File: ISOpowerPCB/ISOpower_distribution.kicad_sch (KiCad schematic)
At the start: 27 parts, among them M1 Fan_IEC60617, Q2 IRF5305_PBF, Q3 IRF5305_PBF, U10 LM2596S-5, U4 i6A4W020A-DC-DC-250W, U5 i6A4W020A-DC-DC-250W, U6 ACS712xLCTR-30A, U7 ACS712xLCTR-30A

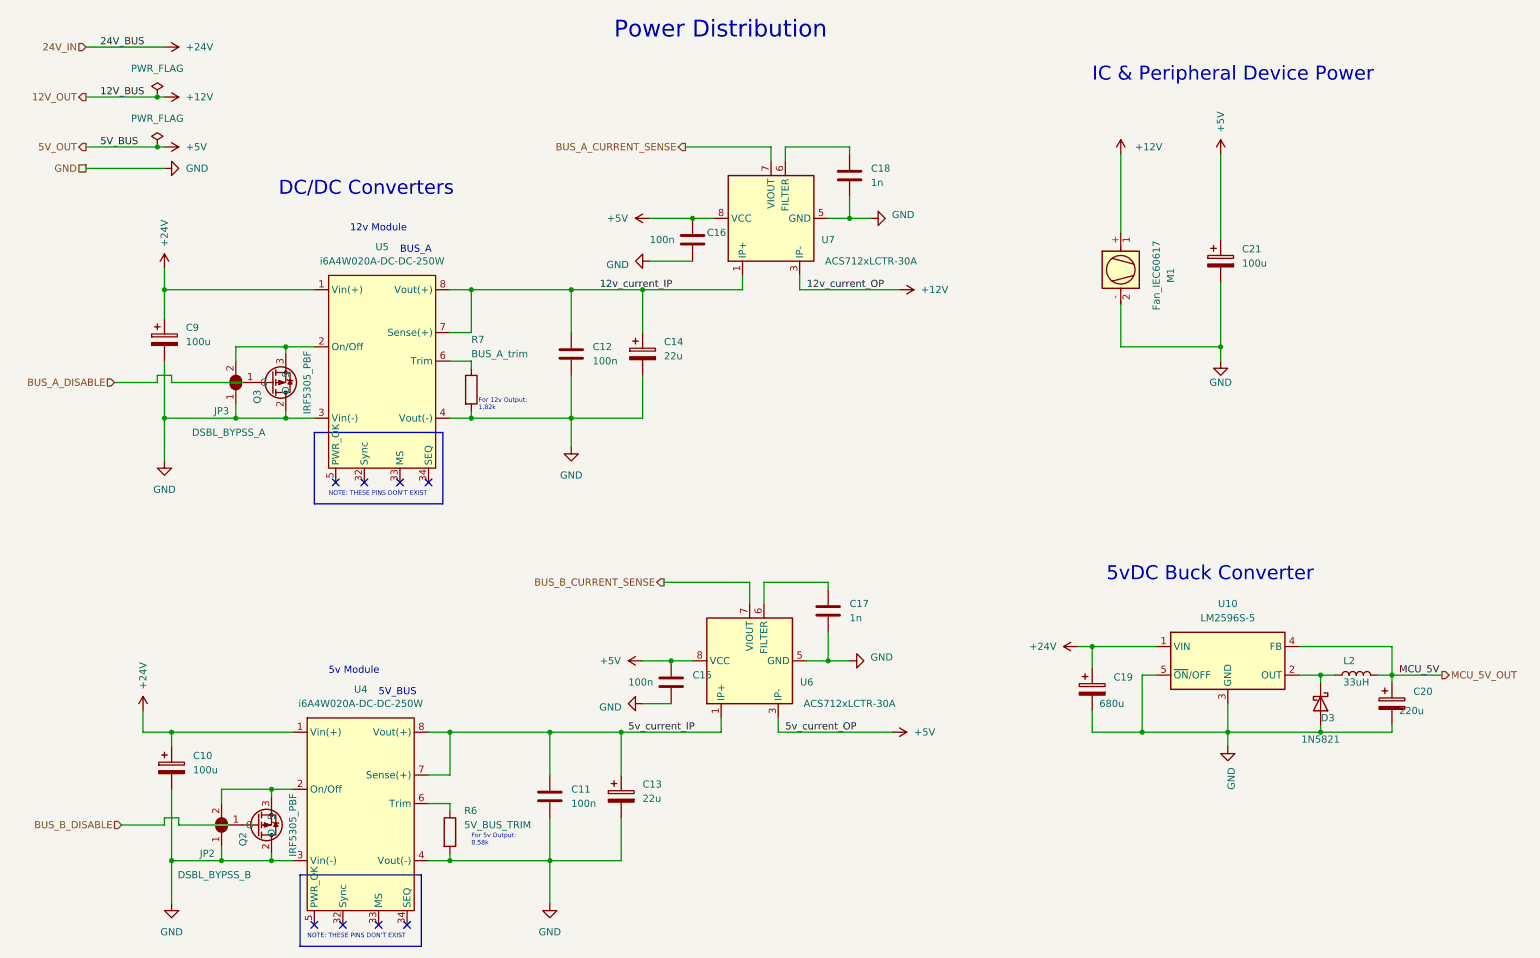
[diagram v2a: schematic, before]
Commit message: added netclasses
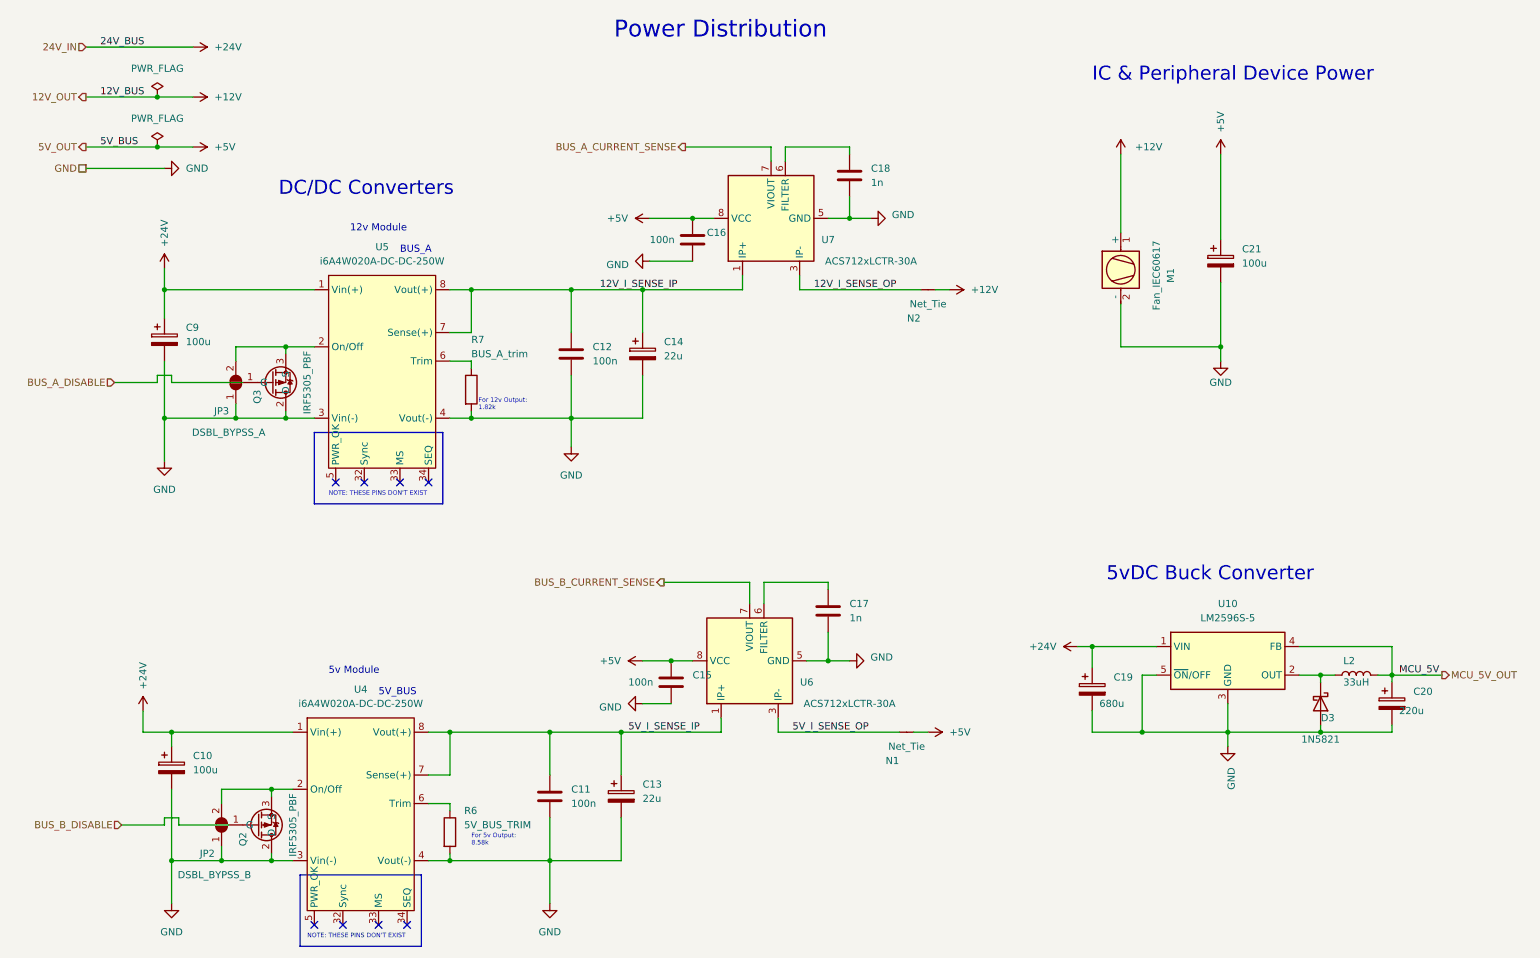
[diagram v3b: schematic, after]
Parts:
- added N1, N2: Net_Tie, NetTie:NetTie-2_SMD_Pad0.5mm, symbol 000_Utility_Immo:Net_Tie
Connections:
- net +12V: now also N2.2 (C); no longer U7.3 (IP-), U7.4 (IP-)
- net +5V: now also N1.2 (C); no longer U6.3 (IP-), U6.4 (IP-)
- net 12v_current_IP renamed 12V_I_SENSE_IP
- net 5v_current_IP renamed 5V_I_SENSE_IP
- new net 12V_I_SENSE_OP: N2.1 (A), U7.3 (IP-), U7.4 (IP-)
- new net 5V_I_SENSE_OP: N1.1 (A), U6.3 (IP-), U6.4 (IP-)
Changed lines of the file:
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@@
     (stroke (width 0) (type default) (color 0 0 0 0))
   )
-  (wire (pts (xy 149.86 143.51) (xy 170.18 143.51))
+  (wire (pts (xy 149.86 143.51) (xy 171.45 143.51))
     (stroke (width 0) (type default) (color 0 0 0 0))
   )
@@
     (stroke (width 0) (type default) (color 0 0 0 0))
   )
-  (wire (pts (xy 26.67 21.59) (xy 40.64 21.59))
+  (wire (pts (xy 26.67 21.59) (xy 45.72 21.59))
     (stroke (width 0) (type default) (color 0 0 0 0))
   )
@@
     (stroke (width 0) (type default) (color 0 0 0 0))
   )
-  (wire (pts (xy 153.67 64.77) (xy 171.45 64.77))
+  (wire (pts (xy 153.67 64.77) (xy 175.26 64.77))
     (stroke (width 0) (type default) (color 0 0 0 0))
   )
@@
     (stroke (width 0) (type default) (color 0 0 0 0))
   )
+  (wire (pts (xy 176.53 143.51) (xy 173.99 143.51))
+    (stroke (width 0) (type default) (color 0 0 0 0))
+  )
   (wire (pts (xy 59.69 165.1) (xy 59.69 166.37))
     (stroke (width 0) (type default) (color 0 0 0 0))
@@
     (stroke (width 0) (type default) (color 0 0 0 0))
   )
-  (wire (pts (xy 39.37 39.37) (xy 40.64 39.37))
+  (wire (pts (xy 39.37 39.37) (xy 45.72 39.37))
     (stroke (width 0) (type default) (color 0 0 0 0))
   )
@@
     (stroke (width 0) (type default) (color 0 0 0 0))
   )
-  (wire (pts (xy 39.37 30.48) (xy 40.64 30.48))
+  (wire (pts (xy 39.37 30.48) (xy 45.72 30.48))
     (stroke (width 0) (type default) (color 0 0 0 0))
   )
@@
   )
   (wire (pts (xy 158.75 118.11) (xy 158.75 116.84))
+    (stroke (width 0) (type default) (color 0 0 0 0))
+  )
+  (wire (pts (xy 180.34 64.77) (xy 177.8 64.77))
     (stroke (width 0) (type default) (color 0 0 0 0))
   )
@@
     (effects (font (size 1.27 1.27)) (justify left bottom))
   )
-  (label "12v_current_IP" (at 118.11 64.77 0)
+  (label "12V_I_SENSE_IP" (at 118.11 64.77 0)
     (effects (font (size 1.27 1.27)) (justify left bottom))
   )
-  (label "5v_current_OP" (at 151.13 143.51 0)
+  (label "12V_I_SENSE_OP" (at 156.21 64.77 0)
     (effects (font (size 1.27 1.27)) (justify left bottom))
   )
-  (label "12v_current_OP" (at 154.94 64.77 0)
+  (label "5V_I_SENSE_OP" (at 152.4 143.51 0)
     (effects (font (size 1.27 1.27)) (justify left bottom))
   )
@@
     (effects (font (size 1.27 1.27)) (justify left bottom))
   )
-  (label "5v_current_IP" (at 123.19 143.51 0)
+  (label "5V_I_SENSE_IP" (at 123.19 143.51 0)
     (effects (font (size 1.27 1.27)) (justify left bottom))
   )
@@
     (pin "1")
   )
-  (symbol (lib_id "power:+5V") (at 170.18 143.51 270) (unit 1)
-    (in_bom yes) (on_board yes)
-    (property "Reference" "#PWR043" (id 0) (at 166.37 143.51 0)
-      (effects (font (size 1.27 1.27)) hide)
-    )
-    (property "Value" "+5V" (id 1) (at 177.8 143.51 90)
-      (effects (font (size 1.27 1.27)) (justify right))
-    )
-    (property "Footprint" "" (id 2) (at 170.18 143.51 0)
-      (effects (font (size 1.27 1.27)) hide)
-    )
-    (property "Datasheet" "" (id 3) (at 170.18 143.51 0)
-      (effects (font (size 1.27 1.27)) hide)
-    )
-    (pin "1")
-  )
-  (symbol (lib_id "power:+24V") (at 40.64 21.59 270) (unit 1)
-    (in_bom yes) (on_board yes)
-    (property "Reference" "#PWR030" (id 0) (at 36.83 21.59 0)
-      (effects (font (size 1.27 1.27)) hide)
-    )
-    (property "Value" "+24V" (id 1) (at 44.45 21.59 90)
-      (effects (font (size 1.27 1.27)) (justify left))
-    )
-    (property "Footprint" "" (id 2) (at 40.64 21.59 0)
-      (effects (font (size 1.27 1.27)) hide)
-    )
-    (property "Datasheet" "" (id 3) (at 40.64 21.59 0)
+  (symbol (lib_id "000_Utility_Immo:Net_Tie") (at 176.53 64.77 0) (unit 1)
+    (in_bom no) (on_board yes)
+    (property "Reference" "N2" (id 0) (at 173.99 69.85 0))
+    (property "Value" "Net_Tie" (id 1) (at 176.53 67.31 0))
+    (property "Footprint" "NetTie:NetTie-2_SMD_Pad0.5mm" (id 2) (at 176.53 67.31 0)
+      (effects (font (size 1.27 1.27)) hide)
+    )
+    (property "Datasheet" "~" (id 3) (at 176.53 63.5 0)
+      (effects (font (size 1.27 1.27)) hide)
+    )
+    (pin "1")
+    (pin "2")
+  )
+  (symbol (lib_id "power:+24V") (at 45.72 21.59 270) (unit 1)
+    (in_bom yes) (on_board yes)
+    (property "Reference" "#PWR030" (id 0) (at 41.91 21.59 0)
+      (effects (font (size 1.27 1.27)) hide)
+    )
+    (property "Value" "+24V" (id 1) (at 49.53 21.59 90)
+      (effects (font (size 1.27 1.27)) (justify left))
+    )
+    (property "Footprint" "" (id 2) (at 45.72 21.59 0)
+      (effects (font (size 1.27 1.27)) hide)
+    )
+    (property "Datasheet" "" (id 3) (at 45.72 21.59 0)
       (effects (font (size 1.27 1.27)) hide)
     )
@@
     (pin "1")
   )
-  (symbol (lib_id "power:+5V") (at 40.64 39.37 270) (unit 1)
-    (in_bom yes) (on_board yes) (fields_autoplaced)
-    (property "Reference" "#PWR032" (id 0) (at 36.83 39.37 0)
-      (effects (font (size 1.27 1.27)) hide)
-    )
-    (property "Value" "+5V" (id 1) (at 44.45 39.3699 90)
-      (effects (font (size 1.27 1.27)) (justify left))
-    )
-    (property "Footprint" "" (id 2) (at 40.64 39.37 0)
-      (effects (font (size 1.27 1.27)) hide)
-    )
-    (property "Datasheet" "" (id 3) (at 40.64 39.37 0)
+  (symbol (lib_id "power:+5V") (at 45.72 39.37 270) (unit 1)
+    (in_bom yes) (on_board yes) (fields_autoplaced)
+    (property "Reference" "#PWR032" (id 0) (at 41.91 39.37 0)
+      (effects (font (size 1.27 1.27)) hide)
+    )
+    (property "Value" "+5V" (id 1) (at 49.53 39.3699 90)
+      (effects (font (size 1.27 1.27)) (justify left))
+    )
+    (property "Footprint" "" (id 2) (at 45.72 39.37 0)
+      (effects (font (size 1.27 1.27)) hide)
+    )
+    (property "Datasheet" "" (id 3) (at 45.72 39.37 0)
       (effects (font (size 1.27 1.27)) hide)
     )
@@
     (pin "2")
   )
-  (symbol (lib_id "power:+12V") (at 171.45 64.77 270) (unit 1)
-    (in_bom yes) (on_board yes) (fields_autoplaced)
-    (property "Reference" "#PWR044" (id 0) (at 167.64 64.77 0)
-      (effects (font (size 1.27 1.27)) hide)
-    )
-    (property "Value" "+12V" (id 1) (at 175.26 64.7699 90)
-      (effects (font (size 1.27 1.27)) (justify left))
-    )
-    (property "Footprint" "" (id 2) (at 171.45 64.77 0)
-      (effects (font (size 1.27 1.27)) hide)
-    )
-    (property "Datasheet" "" (id 3) (at 171.45 64.77 0)
-      (effects (font (size 1.27 1.27)) hide)
-    )
-    (pin "1")
-  )
   (symbol (lib_id "000_Capacitor_Electrolytic_Immo:22u") (at 121.92 154.94 0) (unit 1)
     (in_bom yes) (on_board yes) (fields_autoplaced)
@@
     (pin "2")
   )
-  (symbol (lib_id "power:+12V") (at 40.64 30.48 270) (unit 1)
-    (in_bom yes) (on_board yes) (fields_autoplaced)
-    (property "Reference" "#PWR031" (id 0) (at 36.83 30.48 0)
-      (effects (font (size 1.27 1.27)) hide)
-    )
-    (property "Value" "+12V" (id 1) (at 44.45 30.4799 90)
-      (effects (font (size 1.27 1.27)) (justify left))
-    )
-    (property "Footprint" "" (id 2) (at 40.64 30.48 0)
-      (effects (font (size 1.27 1.27)) hide)
-    )
-    (property "Datasheet" "" (id 3) (at 40.64 30.48 0)
+  (symbol (lib_id "power:+12V") (at 45.72 30.48 270) (unit 1)
+    (in_bom yes) (on_board yes) (fields_autoplaced)
+    (property "Reference" "#PWR031" (id 0) (at 41.91 30.48 0)
+      (effects (font (size 1.27 1.27)) hide)
+    )
+    (property "Value" "+12V" (id 1) (at 49.53 30.4799 90)
+      (effects (font (size 1.27 1.27)) (justify left))
+    )
+    (property "Footprint" "" (id 2) (at 45.72 30.48 0)
+      (effects (font (size 1.27 1.27)) hide)
+    )
+    (property "Datasheet" "" (id 3) (at 45.72 30.48 0)
       (effects (font (size 1.27 1.27)) hide)
     )
@@
     )
     (property "Datasheet" "~" (id 3) (at 39.37 39.37 0)
+      (effects (font (size 1.27 1.27)) hide)
+    )
+    (pin "1")
+  )
+  (symbol (lib_id "power:+5V") (at 176.53 143.51 270) (unit 1)
+    (in_bom yes) (on_board yes) (fields_autoplaced)
+    (property "Reference" "#PWR043" (id 0) (at 172.72 143.51 0)
+      (effects (font (size 1.27 1.27)) hide)
+    )
+    (property "Value" "+5V" (id 1) (at 180.34 143.5099 90)
+      (effects (font (size 1.27 1.27)) (justify left))
+    )
+    (property "Footprint" "" (id 2) (at 176.53 143.51 0)
+      (effects (font (size 1.27 1.27)) hide)
+    )
+    (property "Datasheet" "" (id 3) (at 176.53 143.51 0)
       (effects (font (size 1.27 1.27)) hide)
     )
@@
     (pin "2")
   )
+  (symbol (lib_id "power:+12V") (at 180.34 64.77 270) (unit 1)
+    (in_bom yes) (on_board yes) (fields_autoplaced)
+    (property "Reference" "#PWR044" (id 0) (at 176.53 64.77 0)
+      (effects (font (size 1.27 1.27)) hide)
+    )
+    (property "Value" "+12V" (id 1) (at 184.15 64.7699 90)
+      (effects (font (size 1.27 1.27)) (justify left))
+    )
+    (property "Footprint" "" (id 2) (at 180.34 64.77 0)
+      (effects (font (size 1.27 1.27)) hide)
+    )
+    (property "Datasheet" "" (id 3) (at 180.34 64.77 0)
+      (effects (font (size 1.27 1.27)) hide)
+    )
+    (pin "1")
+  )
   (symbol (lib_id "power:+12V") (at 210.82 40.64 0) (unit 1)
     (in_bom yes) (on_board yes) (fields_autoplaced)
@@
     (pin "1")
   )
+  (symbol (lib_id "000_Utility_Immo:Net_Tie") (at 172.72 143.51 0) (unit 1)
+    (in_bom no) (on_board yes)
+    (property "Reference" "N1" (id 0) (at 170.18 148.59 0))
+    (property "Value" "Net_Tie" (id 1) (at 172.72 146.05 0))
+    (property "Footprint" "NetTie:NetTie-2_SMD_Pad0.5mm" (id 2) (at 172.72 146.05 0)
+      (effects (font (size 1.27 1.27)) hide)
+    )
+    (property "Datasheet" "~" (id 3) (at 172.72 142.24 0)
+      (effects (font (size 1.27 1.27)) hide)
+    )
+    (pin "1")
+    (pin "2")
+  )
 )
